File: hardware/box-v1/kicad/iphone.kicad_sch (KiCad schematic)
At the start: 42 parts, among them J201 USB-C iPhone, U201 LT7911D, U202 TPD4E05U06DQA, U203 TPD4E05U06DQA, U204 TPD4E05U06DQA, U205 USBLC6-2SC6, X201 25MHz

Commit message: hardware/box-v1 in English, with an order package
- Everything in hardware/box-v1 is English: netlist.py, the generators,
  the checks, the README, and the regenerated KiCad sheets, SVGs, BOM
  and netlists. Labels are Confirmed / Likely / Unknown; Option A/B.
- netlist.py carries the ordering data of every BOM line: manufacturer,
  MPN, LCSC code with its evidence, JLCPCB class, price estimate, how it
  is assembled. bom.csv has the new columns; check.py rule R11 checks
  them and the selftest plants 12 faults.
- ORDERING.md: what to send a layout and assembly house, what is done
  and what the vendor does (the layout), the LT7911D documents to ask
  Lontium for, fabrication and assembly specs, bring-up tests, cost
  estimates at 10 and 50 boards, and an RFQ template.
- mechanical.py draws the enclosure outline and connector openings
  (svg/mechanical.svg).
- Design fixes: NRST note (4.7k), the end-of-life inductor replaced
  (SRP1038A-100M), the Bob-Smith capacitor rated 2 kV, capacitor ratings
  matched to stocked parts. Open points are listed in the README.

Co-Authored-By: Claude Opus 5.5 <noreply@anthropic.com>
Claude-Session: https://claude.ai/code/session_01EUDgAy5nU6wYzfaiaKBwjy
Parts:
- C201, C202: Confidence Chưa biết -> Unknown; LCSC (none) -> C1549; MPN (none) -> 0402CG180J500NT; Manufacturer (none) -> FH (Guangdong Fenghua)
- C203, C204, C205, C206, C207, C208, C209, C210, C211, C218: Confidence Chắc -> Confirmed; LCSC (none) -> C1525; MPN (none) -> CL05B104KO5NNNC; Manufacturer (none) -> Samsung Electro-Mechanics
- C212, C213, C214: value 10uF 6.3V -> 10uF 10V; Confidence Chắc -> Confirmed; LCSC (none) -> C19702; MPN (none) -> CL10A106KP8NNNC; Manufacturer (none) -> Samsung Electro-Mechanics
- C215: value 1uF -> 1uF 25V; Confidence Chắc -> Confirmed; LCSC (none) -> C52923; MPN (none) -> CL05A105KA5NQNC; Manufacturer (none) -> Samsung Electro-Mechanics
- C216, C217: Confidence Chưa biết -> Unknown; LCSC (none) -> C1525; MPN (none) -> CL05B104KO5NNNC; Manufacturer (none) -> Samsung Electro-Mechanics
- C219: Confidence Chắc -> Confirmed; LCSC (none) -> C15850; MPN (none) -> CL21A106KAYNNNE; Manufacturer (none) -> Samsung Electro-Mechanics
- C220: value 100nF 25V -> 100nF 50V; Confidence Chắc -> Confirmed; LCSC (none) -> C307331; MPN (none) -> CL05B104KB54PNC; Manufacturer (none) -> Samsung Electro-Mechanics
- D201: Confidence Chắc -> Confirmed; LCSC (none) -> C207260; Manufacturer (none) -> Littelfuse
- FB201, FB202: Confidence Chắc -> Confirmed; LCSC (none) -> C85833; Manufacturer (none) -> Murata
- J201: Confidence Chắc -> Confirmed; LCSC (none) -> C134092; MPN Molex 105450-0101 -> 1054500101; Manufacturer (none) -> Molex; Note Chọn ổ 24P đạt USB 3.2 Gen2; ổ 16P (USB 2.0) không có cặp SS -> Use a 24P receptacle rated USB 3.2 Gen2; a 16P (USB 2.0) on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
- R201, R202: Confidence Chắc -> Confirmed; LCSC (none) -> C25879; MPN (none) -> 0402WGF2201TCE; Manufacturer (none) -> UNI-ROYAL (Uniroyal Elec)
- R203: Confidence Chắc -> Confirmed; LCSC (none) -> C25744; MPN (none) -> 0402WGF1002TCE; Manufacturer (none) -> UNI-ROYAL (Uniroyal Elec)
- R204: Confidence Chưa biết -> Unknown; LCSC (none) -> C25744; MPN (none) -> 0402WGF1002TCE; Manufacturer (none) -> UNI-ROYAL (Uniroyal Elec)
- R205: Confidence Chắc -> Confirmed; LCSC (none) -> C25741; MPN (none) -> 0402WGF1003TCE; Manufacturer (none) -> UNI-ROYAL (Uniroyal Elec)
- R206, R207: Confidence Chưa biết -> Unknown; LCSC (none) -> C26083; MPN (none) -> 0402WGF1004TCE; Manufacturer (none) -> UNI-ROYAL (Uniroyal Elec)
- R210: Confidence Chắc -> Confirmed; LCSC (none) -> C25804; MPN (none) -> 0603WAF1002T5E; Manufacturer (none) -> UNI-ROYAL (Uniroyal Elec)
- R211, R212: Confidence Chắc -> Confirmed; LCSC (none) -> C25905; MPN (none) -> 0402WGF5101TCE; Manufacturer (none) -> UNI-ROYAL (Uniroyal Elec)
- TP201, TP202: Confidence Chắc -> Confirmed; MPN (none) -> none (copper test pad); Manufacturer (none) -> -
- U201: Confidence Có thể -> Likely; Manufacturer (none) -> Lontium Semiconductor; Note Datasheet chịu NDA: chỉ vẽ chân theo chức năng; footprint p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 -> Datasheet under NDA: pins drawn by function only; the footp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
- U202, U203, U204: Confidence Chắc -> Confirmed; Manufacturer (none) -> Texas Instruments
- U205: Confidence Chắc -> Confirmed; Manufacturer (none) -> STMicroelectronics
- X201: Confidence Chưa biết -> Unknown; LCSC (none) -> C9006; MPN (none) -> X322525MOB4SI; Manufacturer (none) -> YXC (Yangxing Tech)
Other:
- note added: "2. iPhone USB-C port + LT7911D (DP Alt Mode -> MIPI CSI-2)"
- note added: "Net labels sit on the pin ends (no wires). Pin numbers '?..' = no datasheet yet, must be confirmed before footprint/layout work."
- note removed: "2. Cổng USB-C iPhone + LT7911D (DP Alt Mode -> MIPI CSI-2)"
- note removed: "Nhãn net đặt ngay đầu chân (không vẽ dây). Chân số '?..' = chưa có datasheet, phải xác nhận trước khi làm footprint/layout."
- title: box-v1: USB-C iPhone + LT7911D -> box-v1: iPhone USB-C + LT7911D

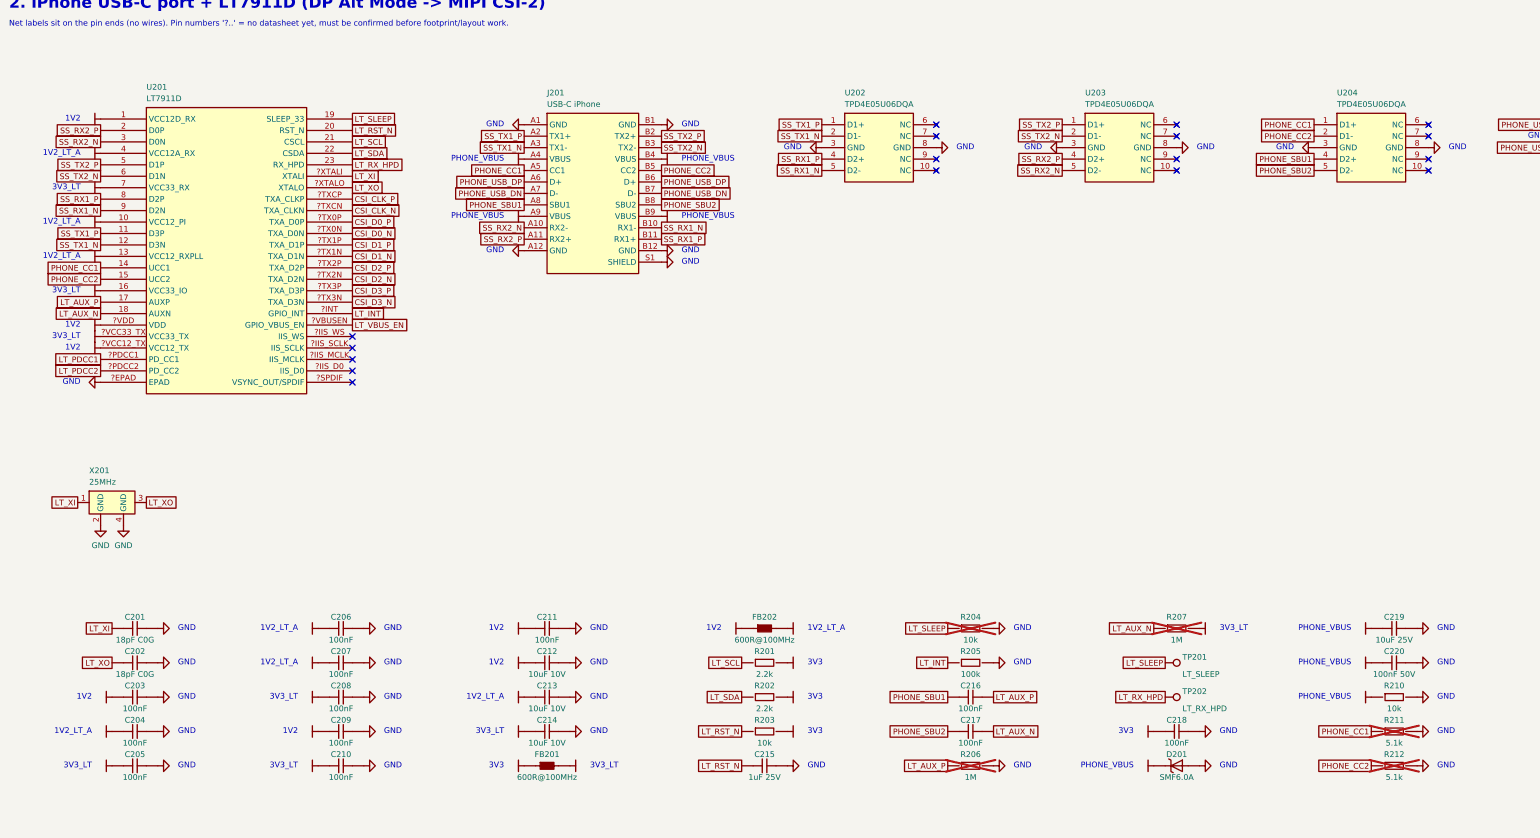
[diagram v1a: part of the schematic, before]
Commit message: Box v1: second design review and a PCB generator
- netlist.py: CH224K VBUS pin left open (R102 removed); D101 SMBJ20A clamps
  below the LMR33630's 36 V input; U107 ESD on the rear CC lines; R213 and a
  100 nF C215 on the LT7911D reset; I2C pull-ups on the module's 3.3 V; J201
  HRO TYPE-C-31-M-04 (hybrid, routable B row); TS-1187A buttons; net classes
  shared with the project file and the board.
- placement.py, pcb.py: the 96x66 mm 4-layer board generated from the
  netlist: footprints (custom LT7911D, Core1106, CH224K, vendored HRO
  receptacle), placement, rules, keep-outs, GND fan-out and stitching,
  Freerouting 1.9 round trip, zones, DRC, compact SVG views.
- mechanical.py follows placement.py; README §11, §14, §15 and ORDERING.md
  describe the layout, the review and the remaining LT7911D work; the
  LT7911D datasheet is public on LCSC.

Co-Authored-By: Claude Opus 5.5 <noreply@anthropic.com>
Claude-Session: https://claude.ai/code/session_01EUDgAy5nU6wYzfaiaKBwjy
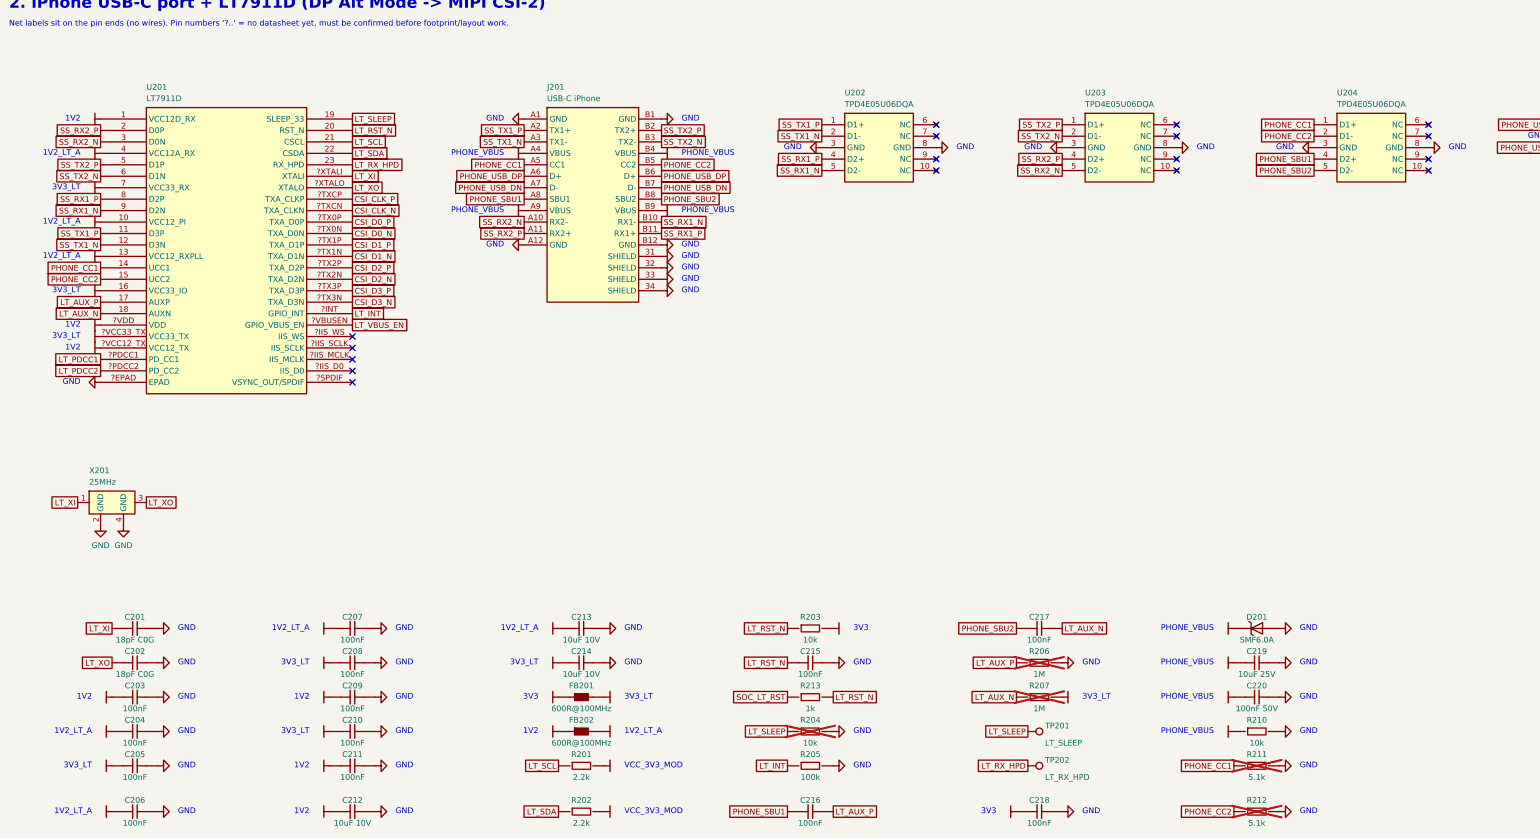
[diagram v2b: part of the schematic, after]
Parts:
- added R213: 1k, Resistor_SMD:R_0402_1005Metric, symbol box-v1:R
- C215: value 1uF 25V -> 100nF; LCSC C52923 -> C1525; MPN CL05A105KA5NQNC -> CL05B104KO5NNNC
- J201: footprint Connector_USB:USB_C_Receptacle_Molex_105450-0101 -> box-v1:USB_C_Receptacle_HRO_TYPE-C-31-M-04; symbol box-v1:USB-C_iPhone_964311 -> box-v1:USB-C_iPhone_595a3e; LCSC C134092 -> C129018; MPN 1054500101 -> TYPE-C-31-M-04; Manufacturer Molex -> Korean Hroparts Elec; Note Use a 24P receptacle rated USB 3.2 Gen2; a 16P (USB 2.0) on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 -> Hybrid: A row SMD, B row through-hole, so the B row is reac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
- U201: Note Datasheet under NDA: pins drawn by function only; the footp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 -> Pins 24-64 are drawn by function only: take them and the fo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
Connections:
- net 3V3: no longer R201.2, R202.2
- net GND: now also J201.31 (SHIELD), J201.32 (SHIELD), J201.33 (SHIELD), J201.34 (SHIELD); no longer J201.S1 (SHIELD)
- net LT_RST_N: now also R213.2
- new net SOC_LT_RST: R213.1
- new net VCC_3V3_MOD: R201.2, R202.2
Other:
- note added: "VCC_3V3_MOD"
- moved on the sheet: C206, C207, C208, C209, C210, C211, C212, C213, C214, C215, C216, C217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
